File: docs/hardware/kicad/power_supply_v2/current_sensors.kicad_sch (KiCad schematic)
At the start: 5 parts, among them U11 INA180A3, U20 INA180A1, U21 INA180A1, U22 INA180A3, U23 INA180A3

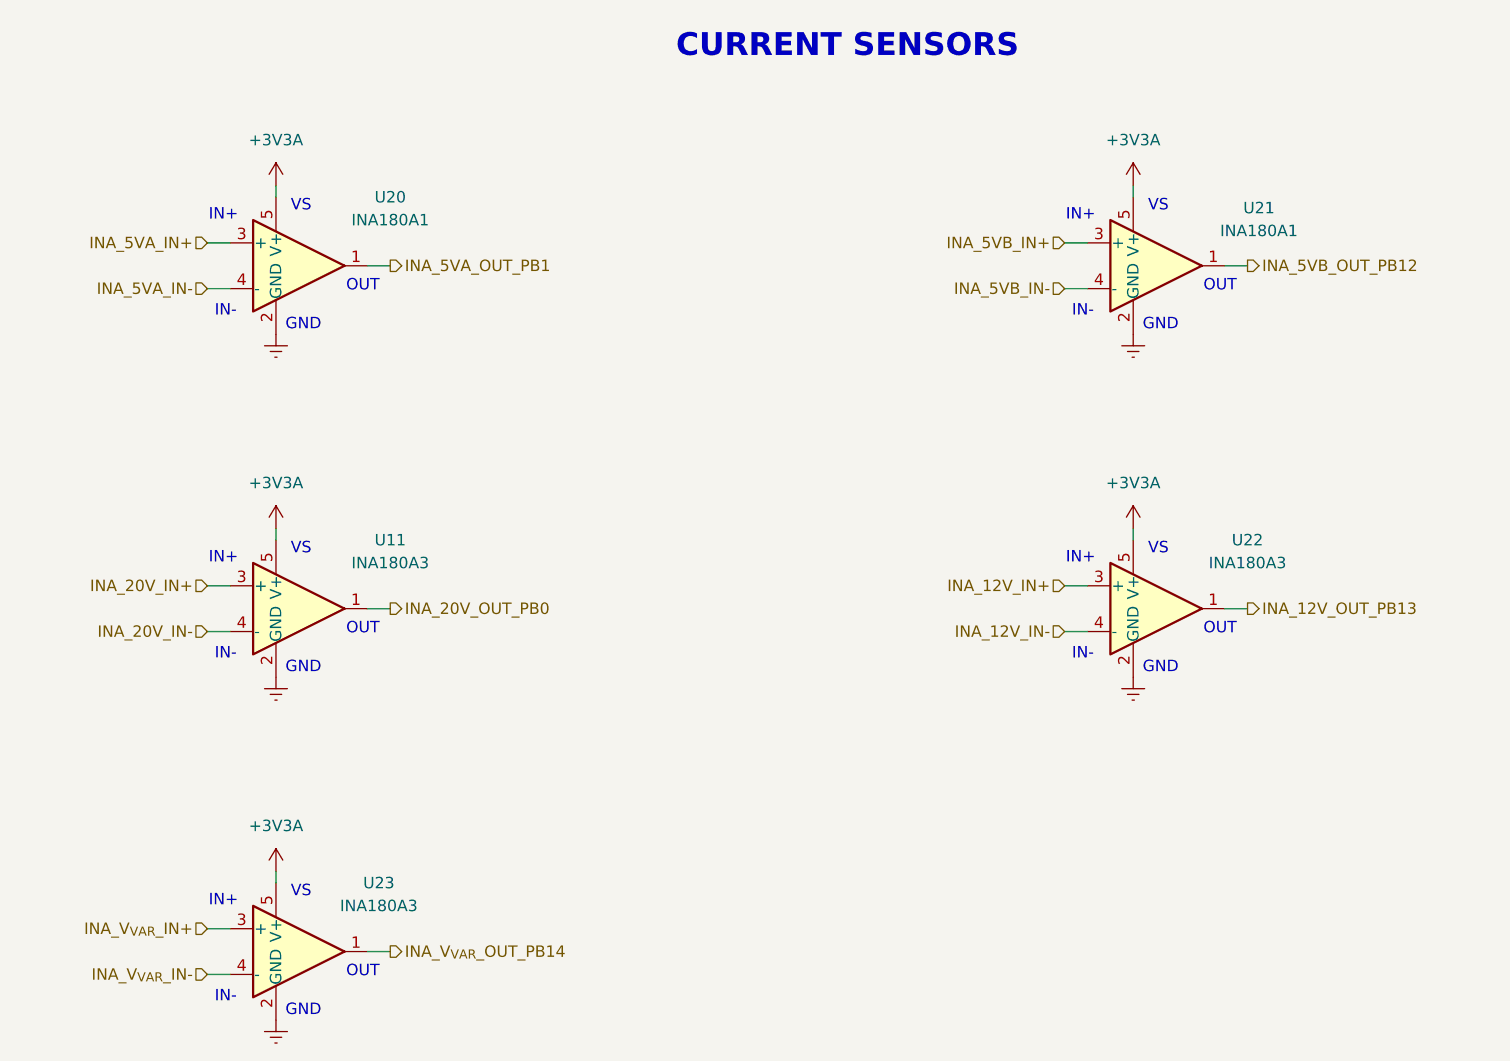
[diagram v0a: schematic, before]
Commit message: updated schematic for LC filters and added voltage injection to other… (#4)
* updated schematic for LC filters and added voltage injection to other bucks

* rework buck resistor divider values + add fb injection to 3V3 and 5V rail bucks

* remove redundant switches for variable rail

* remove datasheets for components no longer used in rev A3

---------

Co-authored-by: chris <chris@laptop.malecki.com>
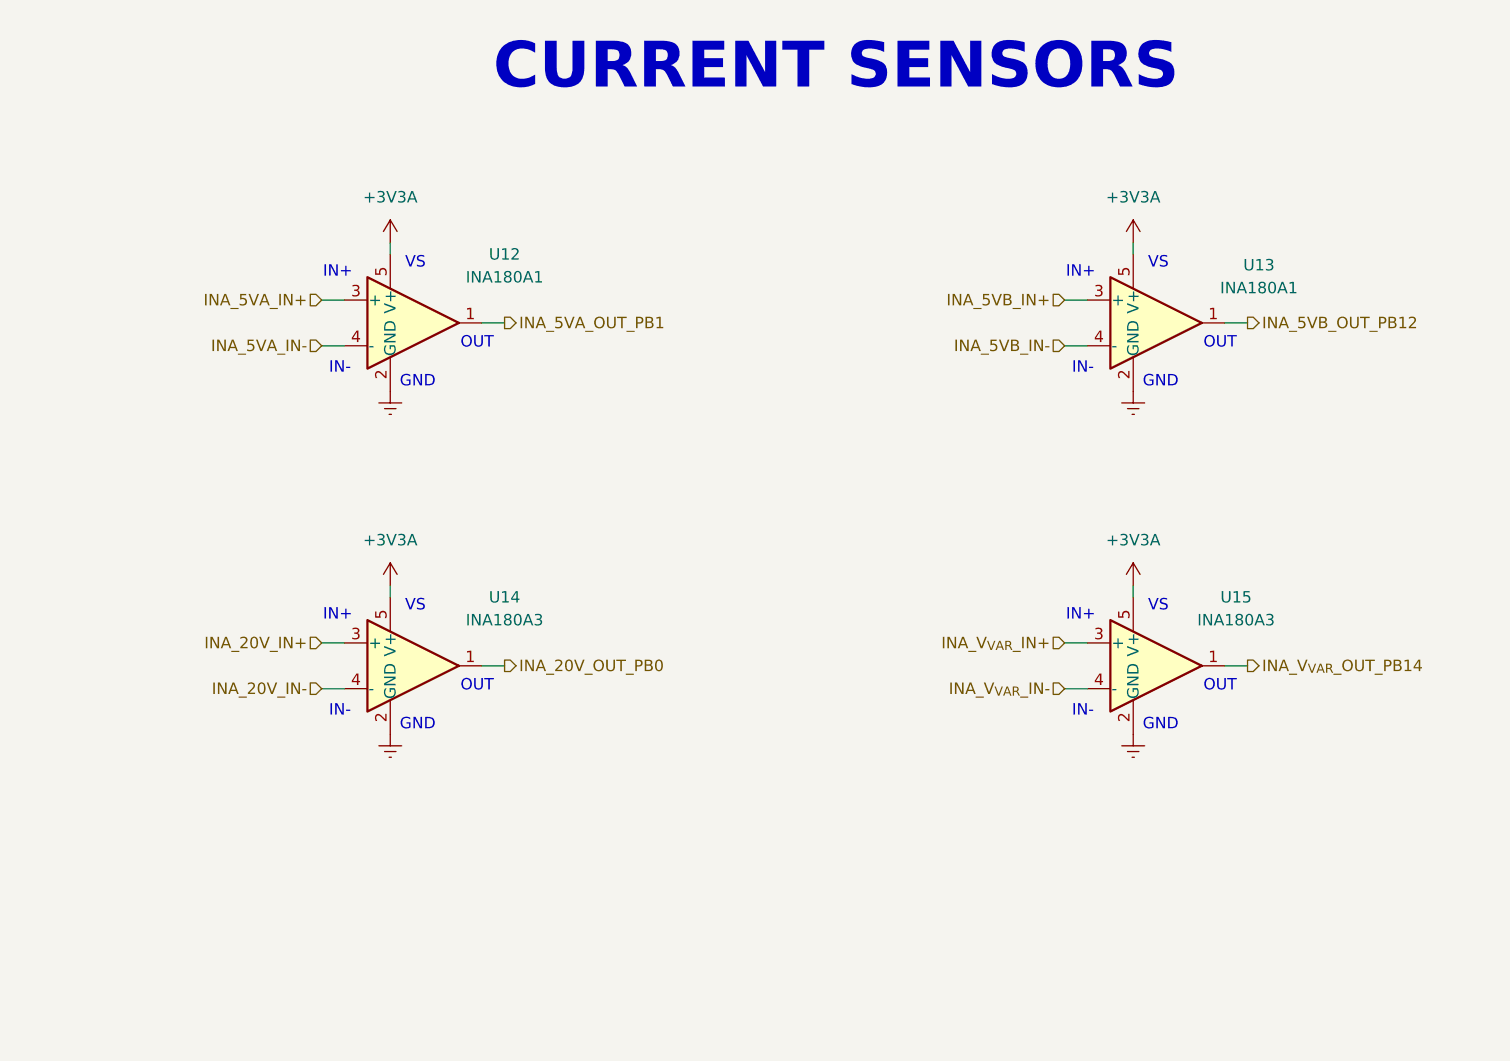
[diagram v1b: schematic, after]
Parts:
- removed U22: INA180A3, Package_TO_SOT_SMD:SOT-23-5, symbol Library:INA180A3
- renumbered U20 to U12, U21 to U13, U11 to U14, U23 to U15
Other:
- moved on the sheet: U12, U13, U14, U15
